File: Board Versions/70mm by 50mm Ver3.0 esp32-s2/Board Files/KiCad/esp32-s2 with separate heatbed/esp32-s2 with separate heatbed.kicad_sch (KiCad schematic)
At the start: 54 parts, among them IC1 ESP32-S2FN4R2, J1 PJ-037B, J2 USB4520-03-0-A, J3 TB003-500-P02BE, J4 TB003-500-P02BE, J5 Conn_01x03_Male, Q1 PJD25N06A_L2_00001, U1 LD1117S33TR_SOT223, U2 MAX31855KASA, Y1 ECS-400-15-33B-CTN-TR

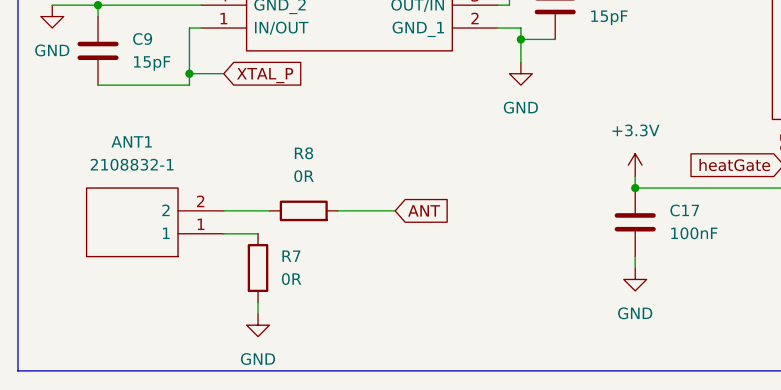
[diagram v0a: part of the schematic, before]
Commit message: Add C for antenna
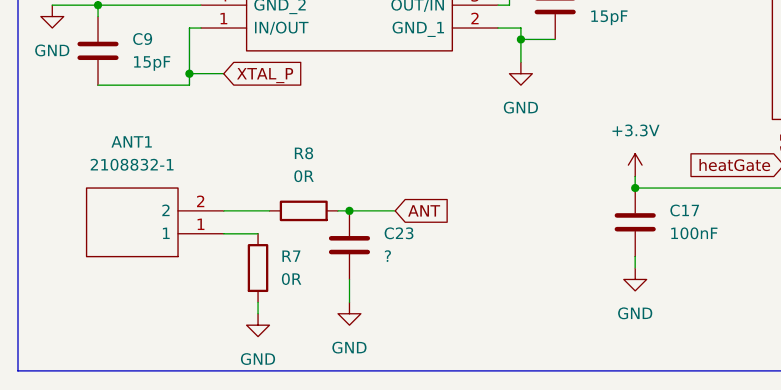
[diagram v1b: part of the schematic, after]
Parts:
- added C23: ?, Capacitor_SMD:C_0603_1608Metric, symbol Device:C
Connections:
- net ANT: now also C23.1
- net GND: now also C23.2
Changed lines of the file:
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@@
   (junction (at 151.13 77.47) (diameter 0) (color 0 0 0 0)
   )
+  (junction (at 53.34 175.26) (diameter 0) (color 0 0 0 0)
+  )
   (junction (at 161.29 40.64) (diameter 0) (color 0 0 0 0)
   )
@@
     (stroke (width 0) (type default) (color 0 0 0 0))
   )
-  (wire (pts (xy 52.07 175.26) (xy 58.42 175.26))
+  (wire (pts (xy 52.07 175.26) (xy 53.34 175.26))
     (stroke (width 0) (type default) (color 0 0 0 0))
   )
@@
     (stroke (width 0) (type default) (color 0 0 0 0))
   )
+  (wire (pts (xy 53.34 182.88) (xy 53.34 185.42))
+    (stroke (width 0) (type default) (color 0 0 0 0))
+  )
   (wire (pts (xy 67.31 21.59) (xy 67.31 27.94))
     (stroke (width 0) (type default) (color 0 0 0 0))
@@
     (stroke (width 0) (type default) (color 0 0 0 0))
   )
+  (wire (pts (xy 53.34 175.26) (xy 58.42 175.26))
+    (stroke (width 0) (type default) (color 0 0 0 0))
+  )
   (wire (pts (xy 132.08 48.26) (xy 143.51 48.26))
     (stroke (width 0) (type default) (color 0 0 0 0))
@@
     (pin "1")
   )
+  (symbol (lib_id "power:GND") (at 53.34 185.42 0) (unit 1)
+    (in_bom yes) (on_board yes) (fields_autoplaced)
+    (property "Reference" "#PWR01" (id 0) (at 53.34 191.77 0)
+      (effects (font (size 1.27 1.27)) hide)
+    )
+    (property "Value" "GND" (id 1) (at 53.34 190.5 0))
+    (property "Footprint" "" (id 2) (at 53.34 185.42 0)
+      (effects (font (size 1.27 1.27)) hide)
+    )
+    (property "Datasheet" "" (id 3) (at 53.34 185.42 0)
+      (effects (font (size 1.27 1.27)) hide)
+    )
+    (pin "1")
+  )
   (symbol (lib_id "Device:R") (at 204.47 93.98 0) (unit 1)
     (in_bom yes) (on_board yes) (fields_autoplaced)
@@
     (pin "2")
   )
+  (symbol (lib_id "Device:C") (at 53.34 179.07 0) (unit 1)
+    (in_bom yes) (on_board yes) (fields_autoplaced)
+    (property "Reference" "C23" (id 0) (at 57.15 177.7999 0)
+      (effects (font (size 1.27 1.27)) (justify left))
+    )
+    (property "Value" "?" (id 1) (at 57.15 180.3399 0)
+      (effects (font (size 1.27 1.27)) (justify left))
+    )
+    (property "Footprint" "Capacitor_SMD:C_0603_1608Metric" (id 2) (at 54.3052 182.88 0)
+      (effects (font (size 1.27 1.27)) hide)
+    )
+    (property "Datasheet" "~" (id 3) (at 53.34 179.07 0)
+      (effects (font (size 1.27 1.27)) hide)
+    )
+    (pin "1")
+    (pin "2")
+  )
   (symbol (lib_id "power:GND") (at 152.4 148.59 0) (unit 1)
     (in_bom yes) (on_board yes) (fields_autoplaced)
@@
   )
   (symbol_instances
+    (path "/d3e4c7bc-b0e0-46a8-9a0f-43bffa203e3c"
+      (reference "#PWR01") (unit 1) (value "GND") (footprint "")
+    )
     (path "/ac12122b-1d13-4255-8ad4-d3c23f563c9c"
       (reference "#PWR0101") (unit 1) (value "GND") (footprint "")
@@
       (reference "C22") (unit 1) (value "100nF") (footprint "Capacitor_SMD:C_0603_1608Metric")
     )
+    (path "/d9970ccc-0f14-4cf4-a36f-78122c353262"
+      (reference "C23") (unit 1) (value "?") (footprint "Capacitor_SMD:C_0603_1608Metric")
+    )
     (path "/648ac16b-9a76-4bd7-a663-a540c11def69"

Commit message: Corrections
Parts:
- removed C3: 22uF, Capacitor_SMD:C_0805_2012Metric, symbol Device:C
- removed C6: 100nF, Capacitor_SMD:C_0603_1608Metric, symbol Device:C
- added C24: 10nF, Capacitor_SMD:C_0603_1608Metric, symbol Device:C
- C5: value 22uF -> 10uF; footprint Capacitor_SMD:C_0805_2012Metric -> Capacitor_SMD:C_0603_1608Metric
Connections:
- net GND: no longer J4.2, U2.2 (T-)
- net at J4.1, U2.3 (T+): now also C24.1
- new net: C24.2, J4.2, U2.2 (T-)
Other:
- moved on the sheet: C4, C5

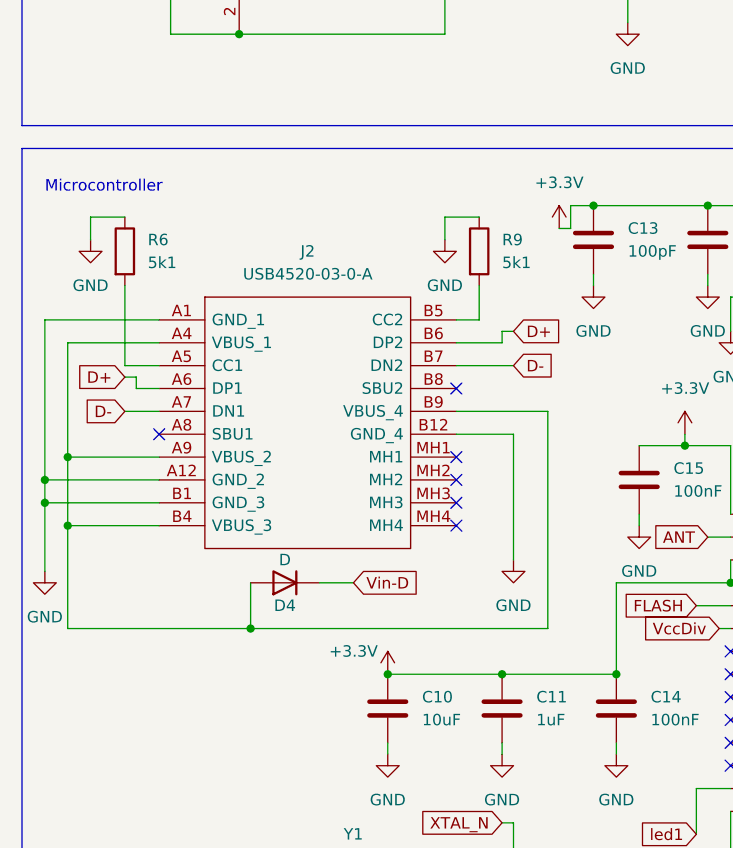
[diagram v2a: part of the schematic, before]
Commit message: Replace wrong USB-C with a correct one
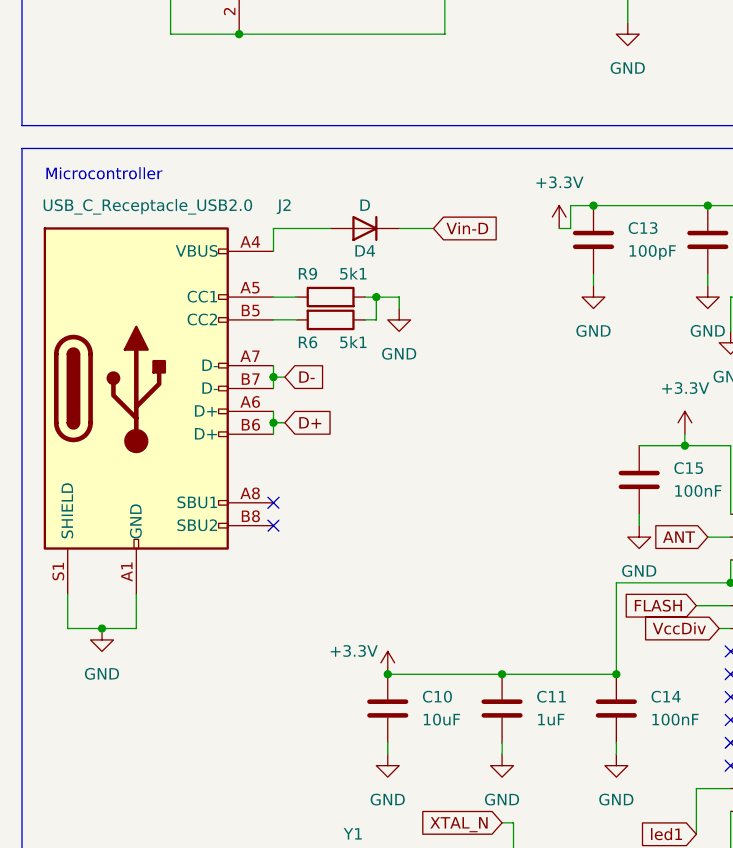
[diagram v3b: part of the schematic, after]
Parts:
- removed J2: USB4520-03-0-A, library_manager:USB4520030A, symbol library_loader:USB4520-03-0-A
- added J2: USB_C_Receptacle_USB2.0, library_manager:TYPE-C-31-M-12, symbol Connector:USB_C_Receptacle_USB2.0
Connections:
- net D+: now also J2.A6 (D+), J2.B6 (D+)
- net D-: now also J2.A7 (D-), J2.B7 (D-)
- net GND: now also R9.2, J2.A1 (GND), J2.A12 (GND), J2.B1 (GND), J2.B12 (GND), J2.S1 (SHIELD); no longer R9.1
- net at D4.2 (A): now also J2.A4 (VBUS), J2.A9 (VBUS), J2.B4 (VBUS), J2.B9 (VBUS)
- net at R6.2: now also J2.B5 (CC2)
- new net: J2.A5 (CC1), R9.1
- no-connect marks 35 -> 31
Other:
- moved on the sheet: D4, R6, R9
